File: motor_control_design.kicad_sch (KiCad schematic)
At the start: 95 parts, among them J1 TYPE-C-31-M-12, J10 5V, J2 SWD, J3 VBAT, J4 GND, J5 FC_M/P, J6 Conn_01x06, J7 Conn_01x04_Pin, J8 Conn_01x06, J9 GND, Q1 RF1S9540SM, Q10 2N7002, Q11 2N7002, Q12 2N7002, Q13 2N7002, Q14 RF1S9540SM, Q15 IRLZ44NS, Q16 2N7002, Q2 RF1S9540SM, Q3 IRLZ44NS, Q4 2N7002, Q5 2N7002, Q6 RF1S9540SM, Q7 IRLZ44NS, Q8 2N7002, Q9 IRLZ44NS, U1 STM32F401CCU6, U2 LT1962-3.3, U3 LTC4365DDB, U4 TPS563200, U5 SSM6N7002KFU_LF, Y1 16MHz

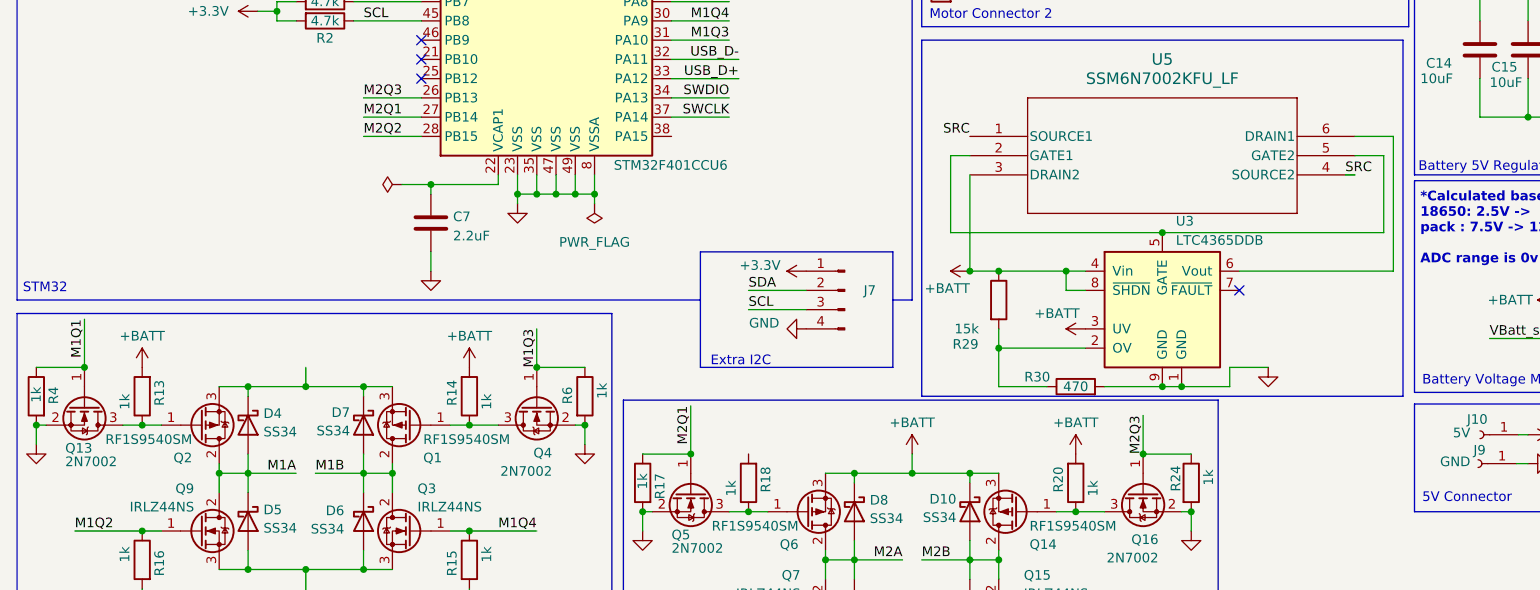
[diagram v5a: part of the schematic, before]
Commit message: vbatt nets
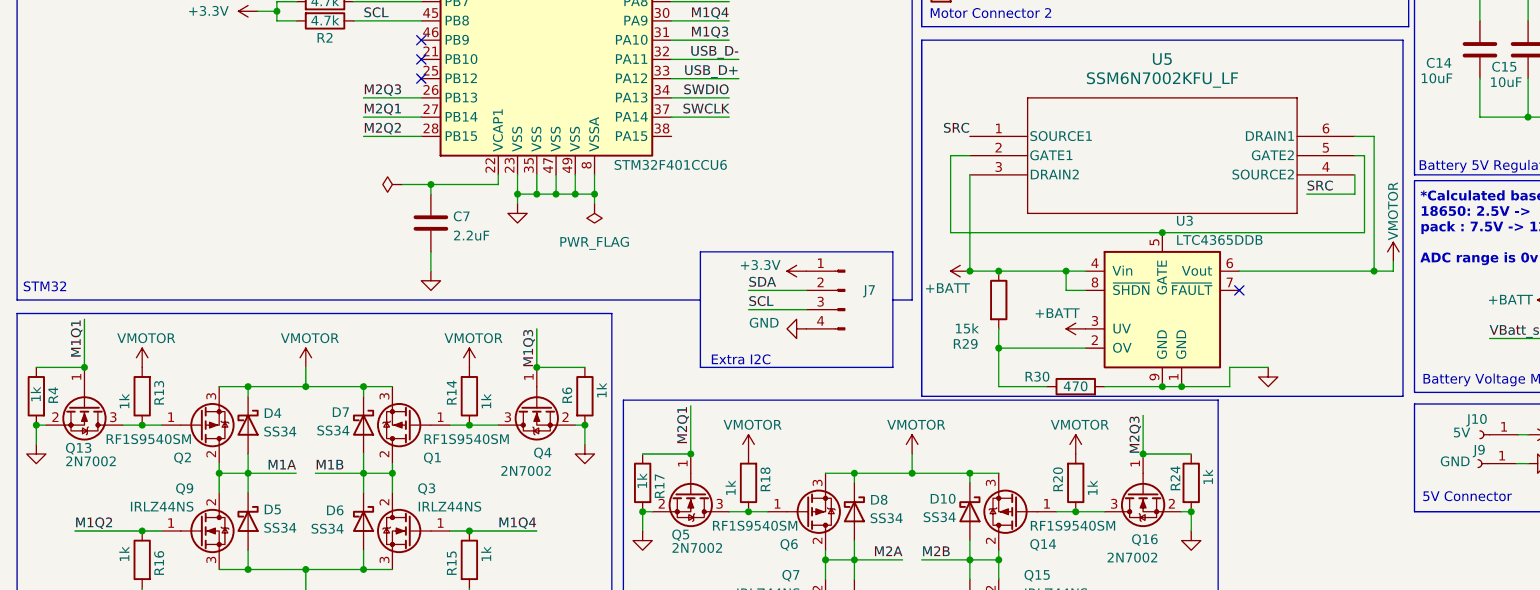
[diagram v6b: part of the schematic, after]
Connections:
- net +BATT: no longer D10.1 (K), D8.1 (K), Q14.3 (S), Q6.3 (S), R13.2, R14.2, R20.2
- net VMOTOR: now reaches D4.1 (K), D7.1 (K), Q1.3 (S), Q2.3 (S)
- net VMOTOR: now also D10.1 (K), D8.1 (K), Q14.3 (S), Q6.3 (S), R13.2, R14.2, R18.2, R20.2, U3.6 (Vout), U5.6 (DRAIN1)

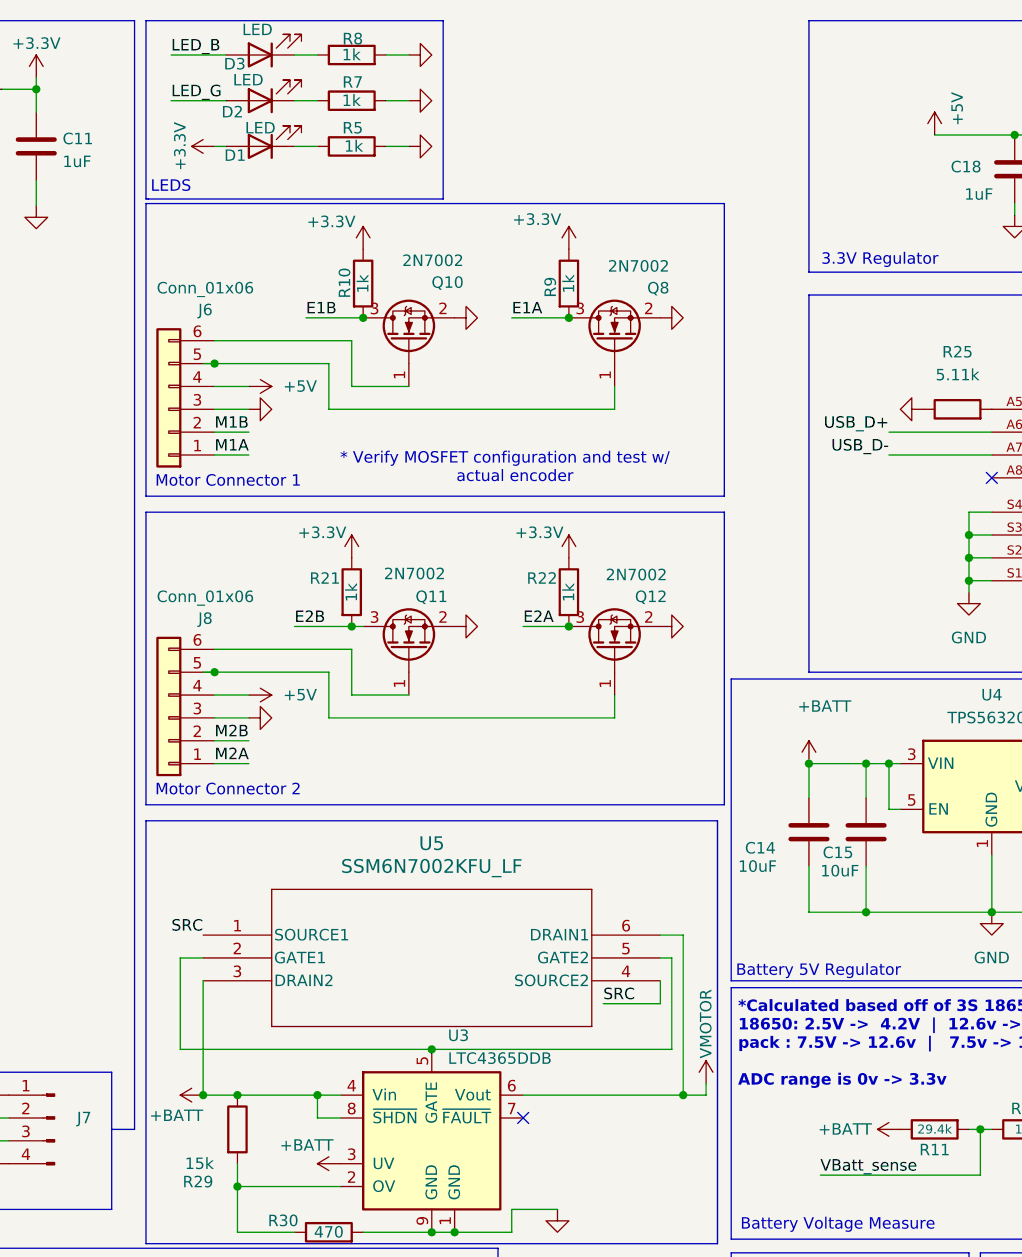
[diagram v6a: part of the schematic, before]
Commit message: schematic tvs diode
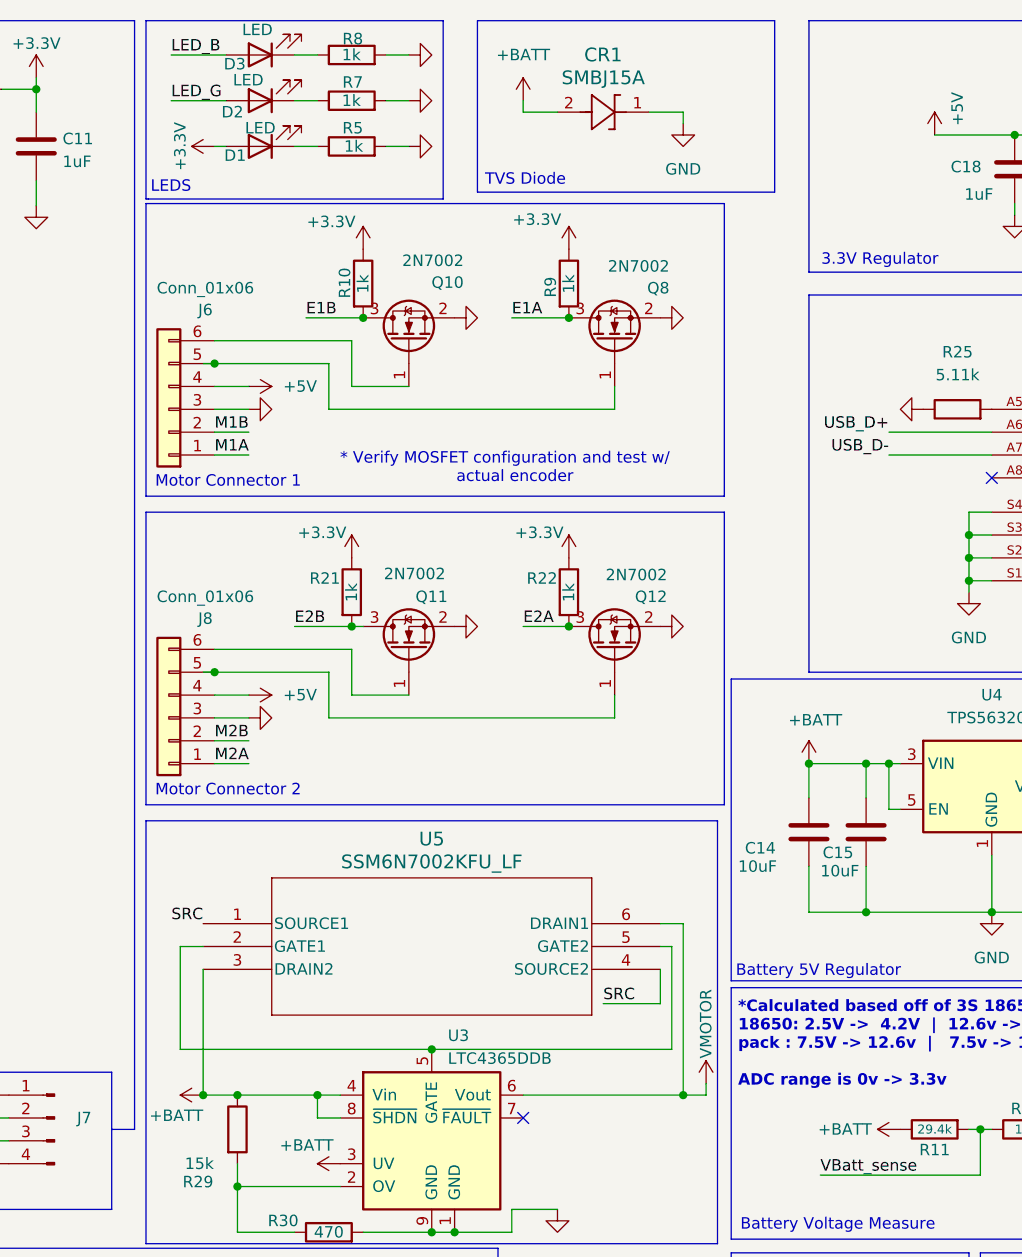
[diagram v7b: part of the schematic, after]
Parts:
- added CR1: SMBJ15A, DO-214AASMB_J-BEND_LTF, symbol Custom:SMBJ15A
- C20: footprint (none) -> Capacitor_SMD:C_0402_1005Metric
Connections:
- net +BATT: now also CR1.2
- net GND: now also CR1.1
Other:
- note added: "TVS Diode"
- moved on the sheet: U5

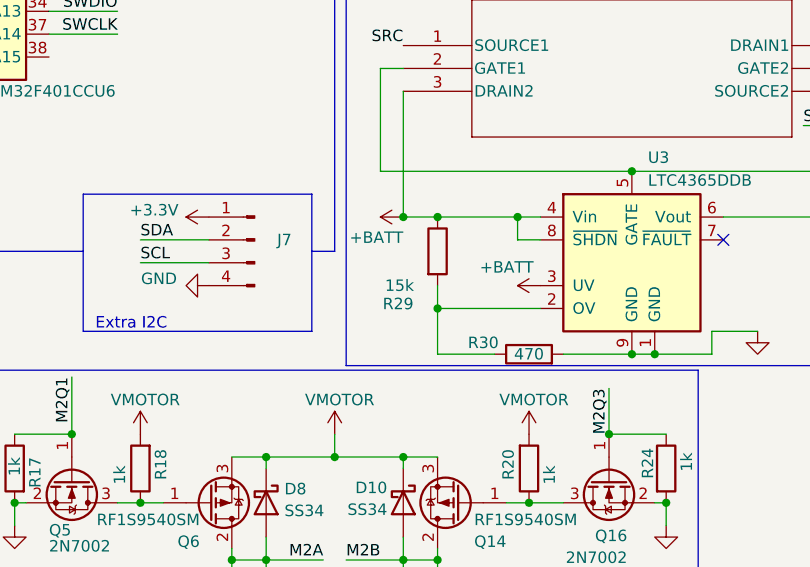
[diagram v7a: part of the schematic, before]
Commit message: layout completed with ov, tvs; only board edge and footprint drc err
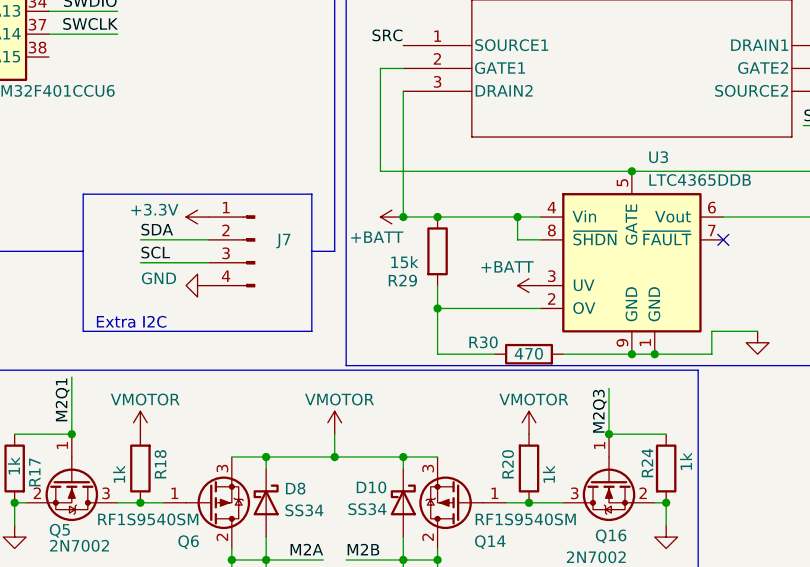
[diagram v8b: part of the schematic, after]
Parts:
- CR1: footprint DO-214AASMB_J-BEND_LTF -> CustomARES:DO-214AASMB_J-BEND_LTF
- R29: footprint (none) -> Resistor_SMD:R_0402_1005Metric
- R30: footprint (none) -> Resistor_SMD:R_0603_1608Metric
- U5: footprint SOT-363 US6_TOS -> CustomARES:SOT-363 US6_TOS-M
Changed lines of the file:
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@@
 			)
 		)
-		(property "Footprint" "DO-214AASMB_J-BEND_LTF"
+		(property "Footprint" "CustomARES:DO-214AASMB_J-BEND_LTF"
 			(at 179.07 24.13 0)
 			(effects
@@
 			)
 		)
-		(property "Footprint" "SOT-363   US6_TOS"
+		(property "Footprint" "CustomARES:SOT-363   US6_TOS-M"
 			(at 139.7 114.3 0)
 			(effects
@@
 		(dnp no)
 		(property "Reference" "R29"
-			(at 137.414 143.002 0)
+			(at 137.922 140.462 0)
 			(effects
 				(font
@@
 		)
 		(property "Value" "15k"
-			(at 137.668 140.97 0)
+			(at 138.176 138.43 0)
 			(effects
 				(font
@@
 			)
 		)
-		(property "Footprint" ""
+		(property "Footprint" "Resistor_SMD:R_0402_1005Metric"
 			(at 141.732 137.16 90)
 			(effects
@@
 			)
 		)
-		(property "Footprint" ""
+		(property "Footprint" "Resistor_SMD:R_0603_1608Metric"
 			(at 153.67 150.368 90)
 			(effects
